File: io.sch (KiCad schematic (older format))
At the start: 17 parts, among them P1 CONN_5, P3 CONN_5, P4 CONN_5, P5 CONN_4, P6 CONN_5, P7 CONN_2, Q1 PDTA124X, Q2 PDTC123Y, U5 VOL617A

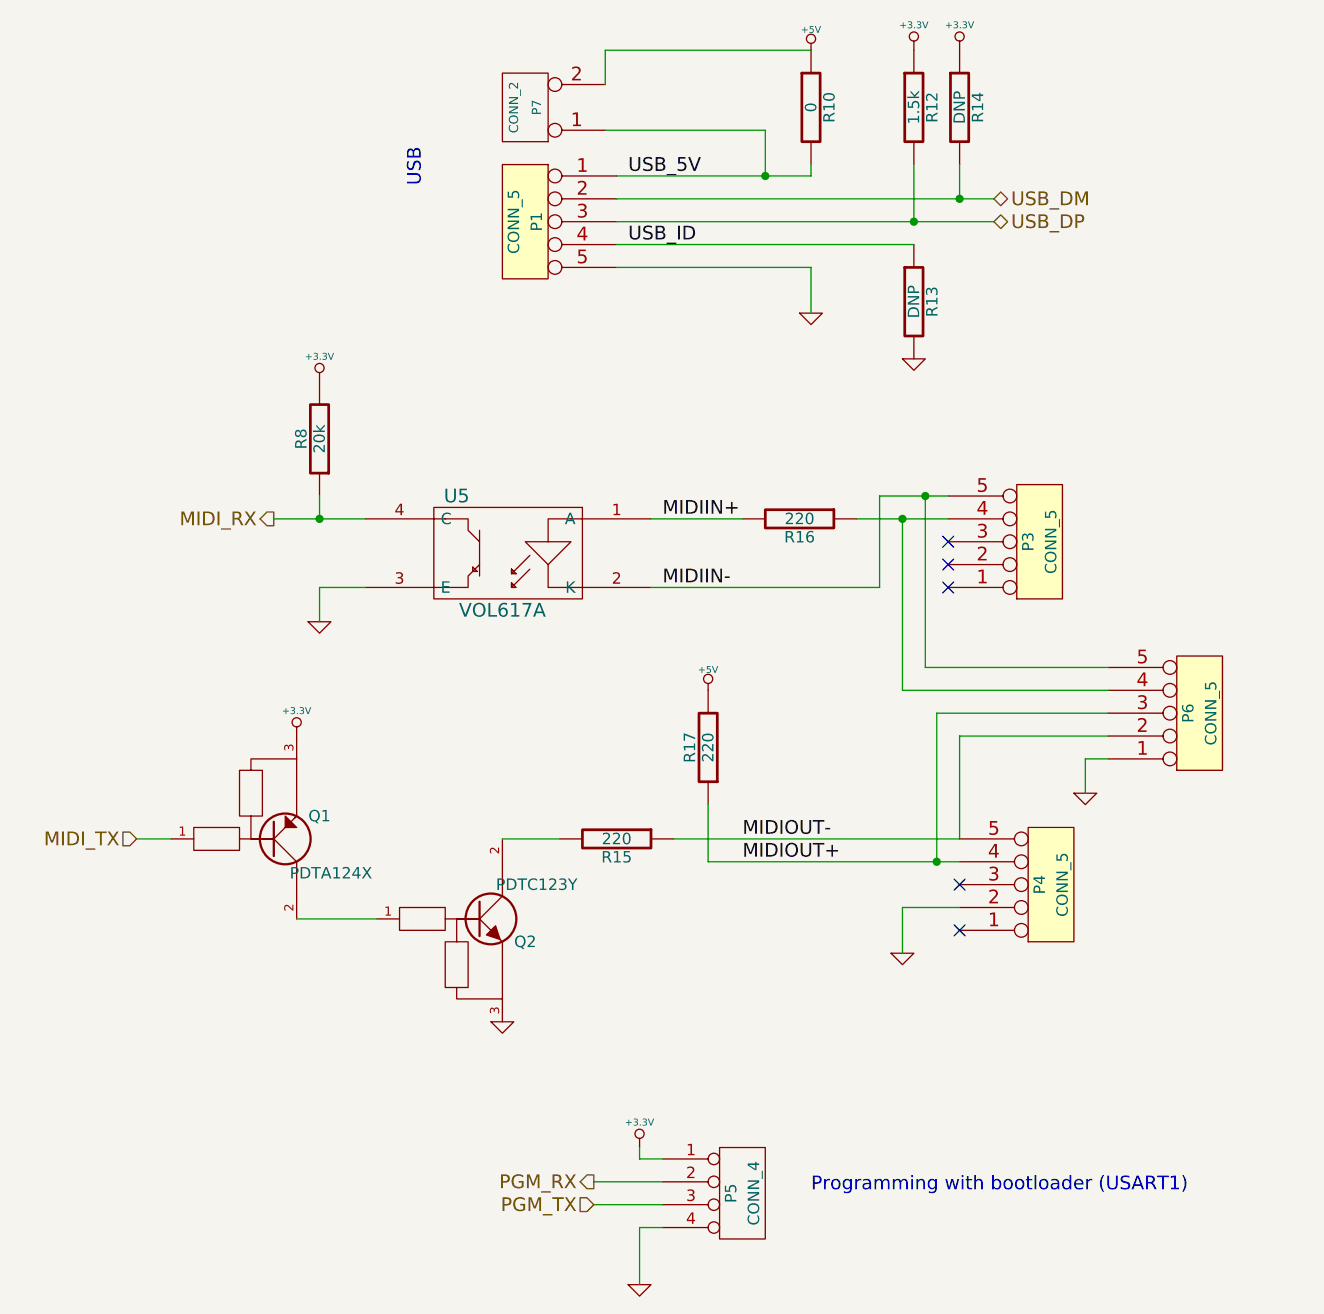
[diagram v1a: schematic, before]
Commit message: Silkscreen updates. Optimisation
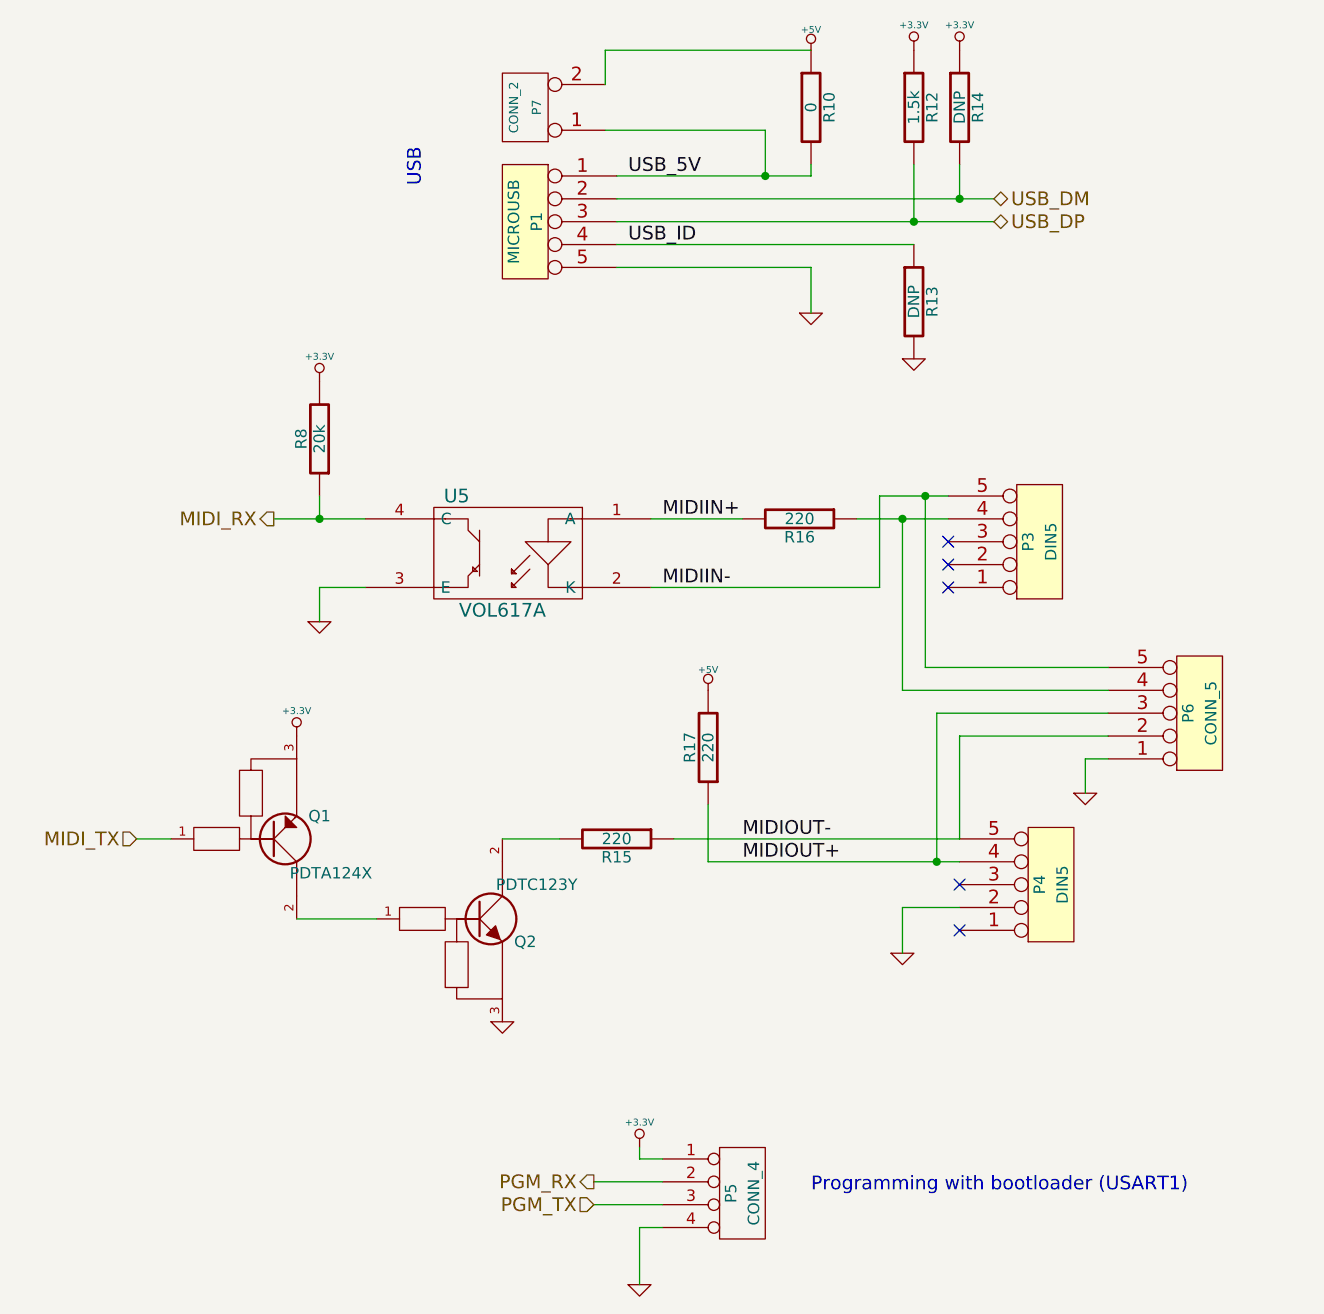
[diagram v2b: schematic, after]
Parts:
- P1: value CONN_5 -> MICROUSB
- P3, P4: value CONN_5 -> DIN5
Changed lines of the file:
@@
-EESchema Schematic File Version 2  date Sat 21 Apr 2012 03:25:21 PM CEST
+EESchema Schematic File Version 2  date Sat 28 Apr 2012 08:49:51 PM CEST
 LIBS:power
 LIBS:device
@@
 $Descr A4 11700 8267
 encoding utf-8
-Sheet 4 8
+Sheet 7 8
 Title ""
-Date "21 apr 2012"
+Date "28 apr 2012"
 Rev ""
 Comp ""
@@
 $EndComp
 $Comp
-L GND #PWR98
+L GND #PWR093
 U 1 1 4F898B55
 P 5400 6350
-F 0 "#PWR98" H 5400 6350 30  0001 C CNN
+F 0 "#PWR093" H 5400 6350 30  0001 C CNN
 F 1 "GND" H 5400 6280 30  0001 C CNN
 	1    5400 6350
@@
 $EndComp
 $Comp
-L +3.3V #PWR97
+L +3.3V #PWR094
 U 1 1 4F898B22
 P 5400 5750
-F 0 "#PWR97" H 5400 5710 30  0001 C CNN
+F 0 "#PWR094" H 5400 5710 30  0001 C CNN
 F 1 "+3.3V" H 5400 5860 30  0000 C CNN
 	1    5400 5750
@@
 $EndComp
 $Comp
-L +3.3V #PWR94
+L +3.3V #PWR095
 U 1 1 4F8985F8
 P 4000 2400
-F 0 "#PWR94" H 4000 2360 30  0001 C CNN
+F 0 "#PWR095" H 4000 2360 30  0001 C CNN
 F 1 "+3.3V" H 4000 2510 30  0000 C CNN
 	1    4000 2400
@@
 $EndComp
 $Comp
-L GND #PWR95
+L GND #PWR096
 U 1 1 4F8984E9
 P 4000 3450
-F 0 "#PWR95" H 4000 3450 30  0001 C CNN
+F 0 "#PWR096" H 4000 3450 30  0001 C CNN
 F 1 "GND" H 4000 3380 30  0001 C CNN
 	1    4000 3450
@@
 $EndComp
 $Comp
-L +3.3V #PWR93
+L +3.3V #PWR097
 U 1 1 4F898360
 P 3900 3950
-F 0 "#PWR93" H 3900 3910 30  0001 C CNN
+F 0 "#PWR097" H 3900 3910 30  0001 C CNN
 F 1 "+3.3V" H 3900 4060 30  0000 C CNN
 	1    3900 3950
@@
 $EndComp
 $Comp
-L GND #PWR96
+L GND #PWR098
 U 1 1 4F897803
 P 4800 5200
-F 0 "#PWR96" H 4800 5200 30  0001 C CNN
+F 0 "#PWR098" H 4800 5200 30  0001 C CNN
 F 1 "GND" H 4800 5130 30  0001 C CNN
 	1    4800 5200
@@
 $EndComp
 $Comp
-L GND #PWR106
+L GND #PWR099
 U 1 1 4F896AAD
 P 7350 4200
-F 0 "#PWR106" H 7350 4200 30  0001 C CNN
+F 0 "#PWR099" H 7350 4200 30  0001 C CNN
 F 1 "GND" H 7350 4130 30  0001 C CNN
 	1    7350 4200
@@
 $EndComp
 $Comp
-L GND #PWR102
+L GND #PWR0100
 U 1 1 4F896A83
 P 6550 4900
-F 0 "#PWR102" H 6550 4900 30  0001 C CNN
+F 0 "#PWR0100" H 6550 4900 30  0001 C CNN
 F 1 "GND" H 6550 4830 30  0001 C CNN
 	1    6550 4900
@@
 P 7200 4600
 F 0 "P4" V 7150 4600 50  0000 C CNN
-F 1 "CONN_5" V 7250 4600 50  0000 C CNN
+F 1 "DIN5" V 7250 4600 50  0000 C CNN
 	1    7200 4600
 	1    0    0    1
@@
 P 7150 3100
 F 0 "P3" V 7100 3100 50  0000 C CNN
-F 1 "CONN_5" V 7200 3100 50  0000 C CNN
+F 1 "DIN5" V 7200 3100 50  0000 C CNN
 	1    7150 3100
 	1    0    0    1
@@
 $EndComp
 $Comp
-L +5V #PWR99
+L +5V #PWR0101
 U 1 1 4F8968A2
 P 5700 3750
-F 0 "#PWR99" H 5700 3840 20  0001 C CNN
+F 0 "#PWR0101" H 5700 3840 20  0001 C CNN
 F 1 "+5V" H 5700 3840 30  0000 C CNN
 	1    5700 3750
@@
 $EndComp
 $Comp
-L GND #PWR104
+L GND #PWR0102
 U 1 1 4F894AD1
 P 6600 2300
-F 0 "#PWR104" H 6600 2300 30  0001 C CNN
+F 0 "#PWR0102" H 6600 2300 30  0001 C CNN
 F 1 "GND" H 6600 2230 30  0001 C CNN
 	1    6600 2300
@@
 $EndComp
 $Comp
-L +3.3V #PWR105
+L +3.3V #PWR0103
 U 1 1 4F894691
 P 6800 950
-F 0 "#PWR105" H 6800 910 30  0001 C CNN
+F 0 "#PWR0103" H 6800 910 30  0001 C CNN
 F 1 "+3.3V" H 6800 1060 30  0000 C CNN
 	1    6800 950
@@
 $EndComp
 $Comp
-L +3.3V #PWR103
+L +3.3V #PWR0104
 U 1 1 4F89446F
 P 6600 950
-F 0 "#PWR103" H 6600 910 30  0001 C CNN
+F 0 "#PWR0104" H 6600 910 30  0001 C CNN
 F 1 "+3.3V" H 6600 1060 30  0000 C CNN
 	1    6600 950
@@
 $EndComp
 $Comp
-L GND #PWR101
+L GND #PWR0105
 U 1 1 4F894376
 P 6150 2100
-F 0 "#PWR101" H 6150 2100 30  0001 C CNN
+F 0 "#PWR0105" H 6150 2100 30  0001 C CNN
 F 1 "GND" H 6150 2030 30  0001 C CNN
 	1    6150 2100
@@
 $EndComp
 $Comp
-L +5V #PWR100
+L +5V #PWR0106
 U 1 1 4F894373
 P 6150 950
-F 0 "#PWR100" H 6150 1040 20  0001 C CNN
+F 0 "#PWR0106" H 6150 1040 20  0001 C CNN
 F 1 "+5V" H 6150 1040 30  0000 C CNN
 	1    6150 950
@@
 P 4900 1700
 F 0 "P1" V 4850 1700 50  0000 C CNN
-F 1 "CONN_5" V 4950 1700 50  0000 C CNN
+F 1 "MICROUSB" V 4950 1700 50  0000 C CNN
 	1    4900 1700
 	-1   0    0    -1
